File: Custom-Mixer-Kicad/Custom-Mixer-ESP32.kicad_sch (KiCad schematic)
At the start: 20 parts, among them J1 OLED1, J2 OLED2, J3 OLED3, J4 OLED4, J5 OLED5, SW1 RotaryEncoder_Switch, SW2 RotaryEncoder_Switch, U1 ESP32-DevKitC, U2 2717

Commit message: Add +3V3 power symbols and update PCB routing
Added multiple +3V3 power symbols to the schematic for improved clarity and power distribution. Updated PCB routing for nets 1 and 7, including new segments, vias, and changes to net connections for better signal integrity and layout. Adjusted positions of Hackclublogo footprints.
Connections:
- net +3V3: now also RV1.3, RV2.3, RV3.3, RV4.3, RV5.3

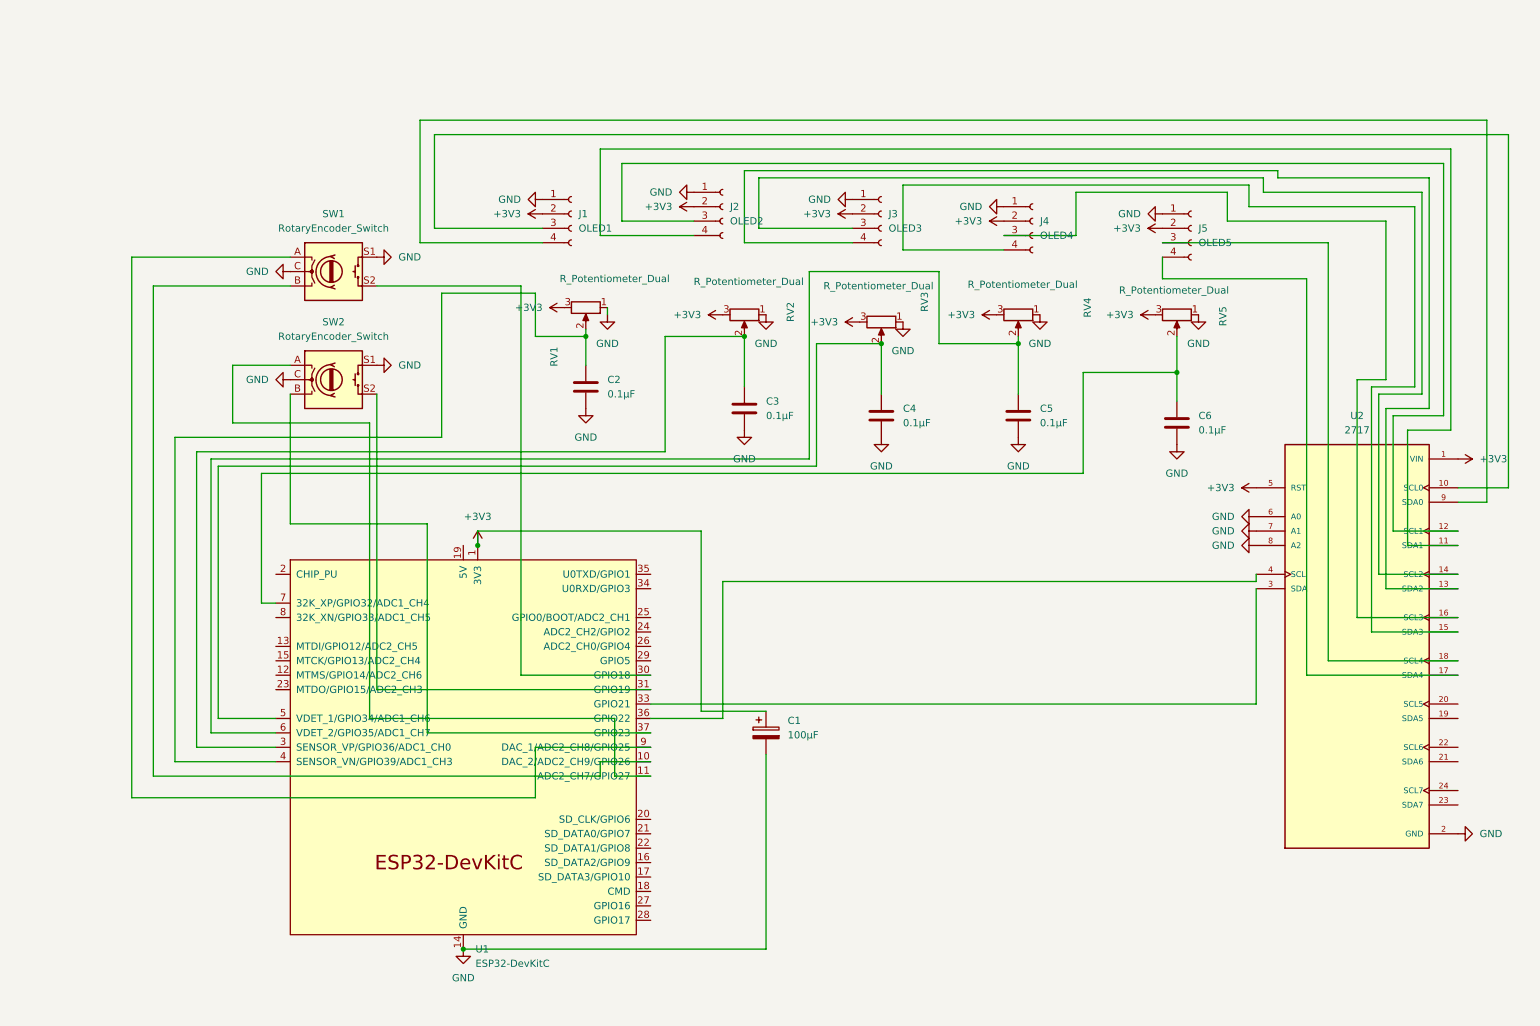
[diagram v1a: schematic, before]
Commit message: Add MCP23017 PCB project & update KiCad libs
Add Adafruit MCP23017 GPIO Expander KiCad project (board, schematic, MCP23017 symbol/footprint, README, license, assets and pretty library parts). Add OLED 128x64 symbol/module files. Modify Custom-Mixer-ESP32 schematic and PCB, and update fp-lib-table and sym-lib-table to include the new parts and libraries.
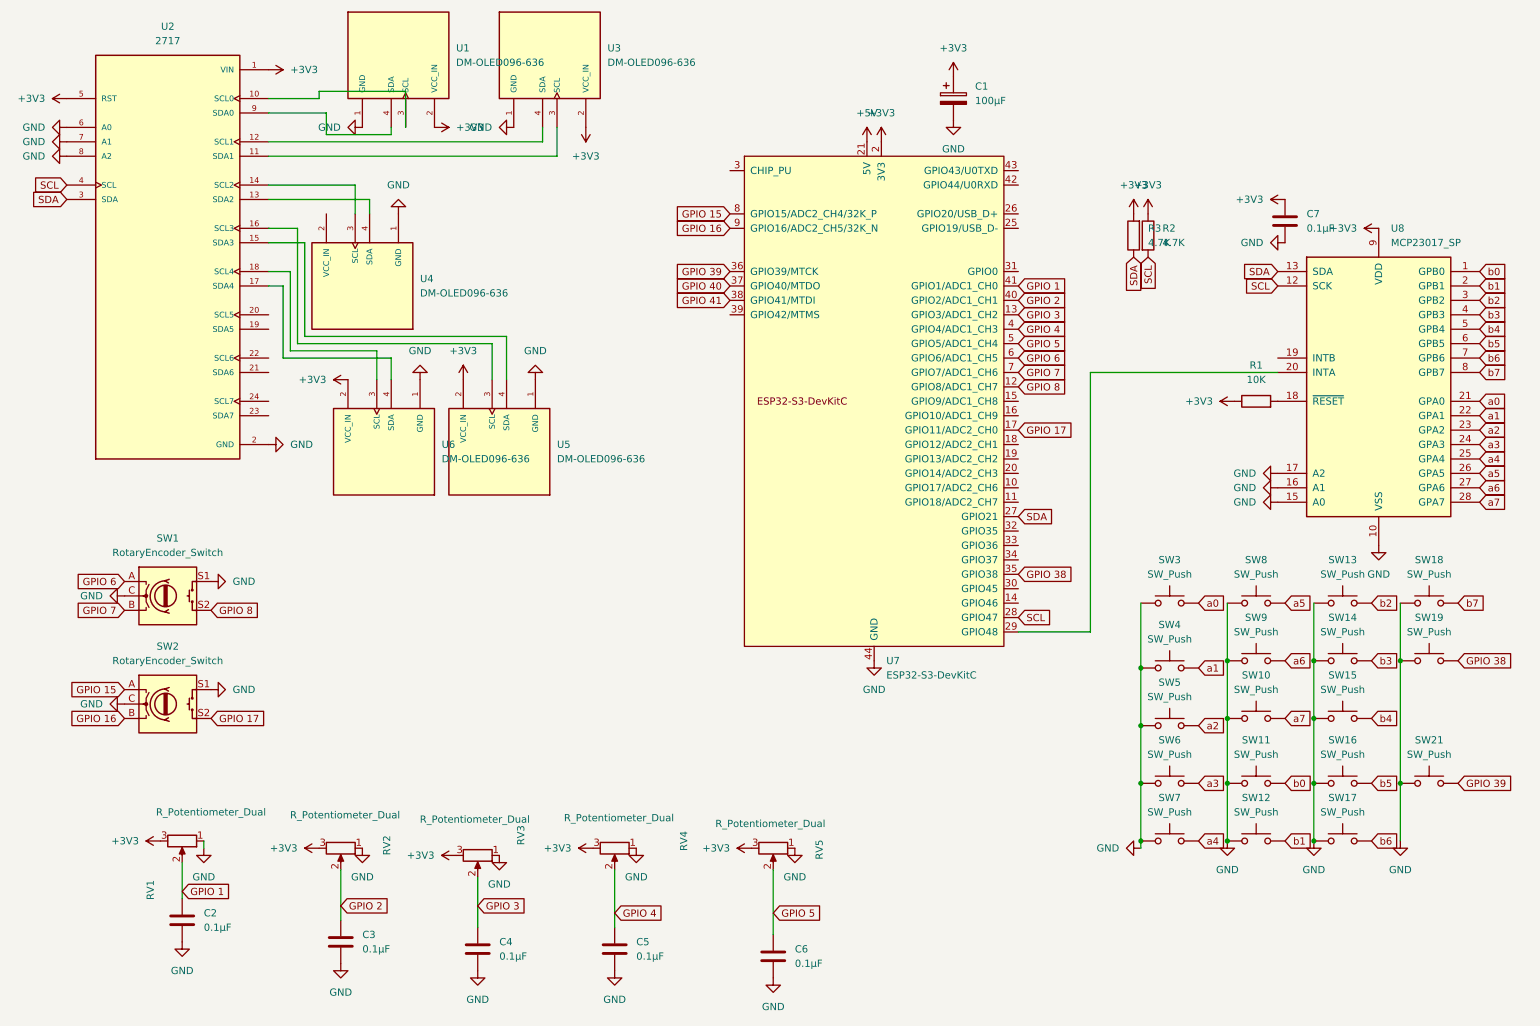
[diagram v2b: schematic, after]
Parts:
- removed J1: OLED1, KiCad-SSD1306-0.91-OLED-4pin-128x32:SSD1306-0.91-OLED-4pin-128x32, symbol Connector:Conn_01x04_Socket
- removed J2: OLED2, KiCad-SSD1306-0.91-OLED-4pin-128x32:SSD1306-0.91-OLED-4pin-128x32, symbol Connector:Conn_01x04_Socket
- removed J3: OLED3, KiCad-SSD1306-0.91-OLED-4pin-128x32:SSD1306-0.91-OLED-4pin-128x32, symbol Connector:Conn_01x04_Socket
- removed J4: OLED4, KiCad-SSD1306-0.91-OLED-4pin-128x32:SSD1306-0.91-OLED-4pin-128x32, symbol Connector:Conn_01x04_Socket
- removed J5: OLED5, KiCad-SSD1306-0.91-OLED-4pin-128x32:SSD1306-0.91-OLED-4pin-128x32, symbol Connector:Conn_01x04_Socket
- removed U1: ESP32-DevKitC, PCM_Espressif:ESP32-DevKitC, symbol PCM_Espressif:ESP32-DevKitC
- added C7: 0.1µF, Capacitor_THT:C_Disc_D5.0mm_W2.5mm_P2.50mm, symbol Device:C
- added R1: 10K, Resistor_THT:R_Axial_DIN0207_L6.3mm_D2.5mm_P7.62mm_Horizontal, symbol Device:R
- added R2, R3: 4.7K, Resistor_THT:R_Axial_DIN0207_L6.3mm_D2.5mm_P7.62mm_Horizontal, symbol Device:R
- added SW10, SW11, SW12, SW13, SW14, SW15, SW16, SW17, SW18, SW19, SW21, SW3, SW4, SW5, SW6, SW7, SW8, SW9: SW_Push, Button_Switch_Keyboard:SW_Cherry_MX_1.00u_PCB, symbol Switch:SW_Push
- added U1, U3, U4, U5, U6: DM-OLED096-636, Oled Screen 128x64:MODULE_DM-OLED096-636, symbol DM-OLED096-636:DM-OLED096-636
- added U7: ESP32-S3-DevKitC, PCM_Espressif:ESP32-S3-DevKitC, symbol PCM_Espressif:ESP32-S3-DevKitC
- added U8: MCP23017_SP, Package_DIP:DIP-28_W7.62mm, symbol Interface_Expansion:MCP23017_SP
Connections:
- net +3V3: now also C7.1, R1.1, R2.1, R3.2, U1.2 (VCC_IN), U3.2 (VCC_IN), U5.2 (VCC_IN), U6.2 (VCC_IN), U7.1 (3V3), U7.2 (3V3), U8.9 (VDD)
- net GND: now also C7.2, SW10.1, SW11.1, SW12.1, SW13.1, SW14.1, SW15.1, SW16.1, SW17.1, SW18.1, SW19.1, SW21.1, SW3.1, SW4.1, SW5.1, SW6.1, SW7.1, SW8.1, SW9.1, U1.1 (GND), U3.1 (GND), U4.1 (GND), U5.1 (GND), U6.1 (GND), U7.22 (GND), U7.23 (GND), U7.24 (GND), U7.44 (GND), U8.10 (VSS), U8.15 (A0), U8.16 (A1), U8.17 (A2)
- net GPIO 3: now reaches C4.1, RV3.2
- net GPIO 3: now also U7.13 (GPIO3/ADC1_CH2)
- net GPIO 4: now reaches C5.1, RV4.2
- net GPIO 4: now also U7.4 (GPIO4/ADC1_CH3)
- net at U2.14 (SCL2): now also U4.3 (SCL)
- net at U2.13 (SDA2): now also U4.4 (SDA)
- net GPIO 2: now reaches C3.1, RV2.2
- net GPIO 2: now also U7.40 (GPIO2/ADC1_CH1)
- net at U2.10 (SCL0): now also U1.3 (SCL)
- net at U2.9 (SDA0): now also U1.4 (SDA)
- net GPIO 5: now reaches C6.1, RV5.2
- net GPIO 5: now also U7.5 (GPIO5/ADC1_CH4)
- net at U2.11 (SDA1): now also U3.3 (SCL)
- net at U2.12 (SCL1): now also U3.4 (SDA)
- net at U2.15 (SDA3): now also U5.4 (SDA)
- net at U2.16 (SCL3): now also U5.3 (SCL)
- net at U2.17 (SDA4): now also U6.4 (SDA)
- net at U2.18 (SCL4): now also U6.3 (SCL)
- net SDA: now reaches U2.3 (SDA)
- net SDA: now also R3.1, U7.27 (GPIO21), U8.13 (SDA)
- net SCL: now reaches U2.4 (SCL)
- net SCL: now also R2.2, U7.28 (GPIO47), U8.12 (SCK)
- net GPIO 7: now reaches SW1.B
- net GPIO 7: now also U7.7 (GPIO7/ADC1_CH6)
- net GPIO 15: now reaches SW2.A
- net GPIO 15: now also U7.8 (GPIO15/ADC2_CH4/32K_P)
- net GPIO 8: now reaches SW1.S2
- net GPIO 8: now also U7.12 (GPIO8/ADC1_CH7)
- net GPIO 17: now reaches SW2.S2
- net GPIO 17: now also U7.17 (GPIO11/ADC2_CH0)
- net GPIO 16: now reaches SW2.B
- net GPIO 16: now also U7.9 (GPIO16/ADC2_CH5/32K_N)
- net GPIO 1: now reaches C2.1, RV1.2
- net GPIO 1: now also U7.41 (GPIO1/ADC1_CH0)
- net GPIO 6: now reaches SW1.A
- net GPIO 6: now also U7.6 (GPIO6/ADC1_CH5)
- new net: U7.29 (GPIO48), U8.20 (INTA)
- new net: R1.2, U8.18 (~{RESET})
- new net +5V: U7.21 (5V)
- new net GPIO 38: SW19.2, U7.35 (GPIO38)
- new net GPIO 39: SW21.2, U7.36 (GPIO39/MTCK)
- new net GPIO 40: U7.37 (GPIO40/MTDO)
- new net GPIO 41: U7.38 (GPIO41/MTDI)
- new net a0: SW3.2, U8.21 (GPA0)
- new net a1: SW4.2, U8.22 (GPA1)
- new net a2: SW5.2, U8.23 (GPA2)
- new net a3: SW6.2, U8.24 (GPA3)
- new net a4: SW7.2, U8.25 (GPA4)
- new net a5: SW8.2, U8.26 (GPA5)
- new net a6: SW9.2, U8.27 (GPA6)
- new net a7: SW10.2, U8.28 (GPA7)
- new net b0: SW11.2, U8.1 (GPB0)
- new net b1: SW12.2, U8.2 (GPB1)
- new net b2: SW13.2, U8.3 (GPB2)
- new net b3: SW14.2, U8.4 (GPB3)
- new net b4: SW15.2, U8.5 (GPB4)
- new net b5: SW16.2, U8.6 (GPB5)
- new net b6: SW17.2, U8.7 (GPB6)
- new net b7: SW18.2, U8.8 (GPB7)
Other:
- moved on the sheet: C1, C2, C3, C4, C5, C6, RV1, RV2, RV3, RV4, RV5, SW1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

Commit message: Rewire and create custom footprint
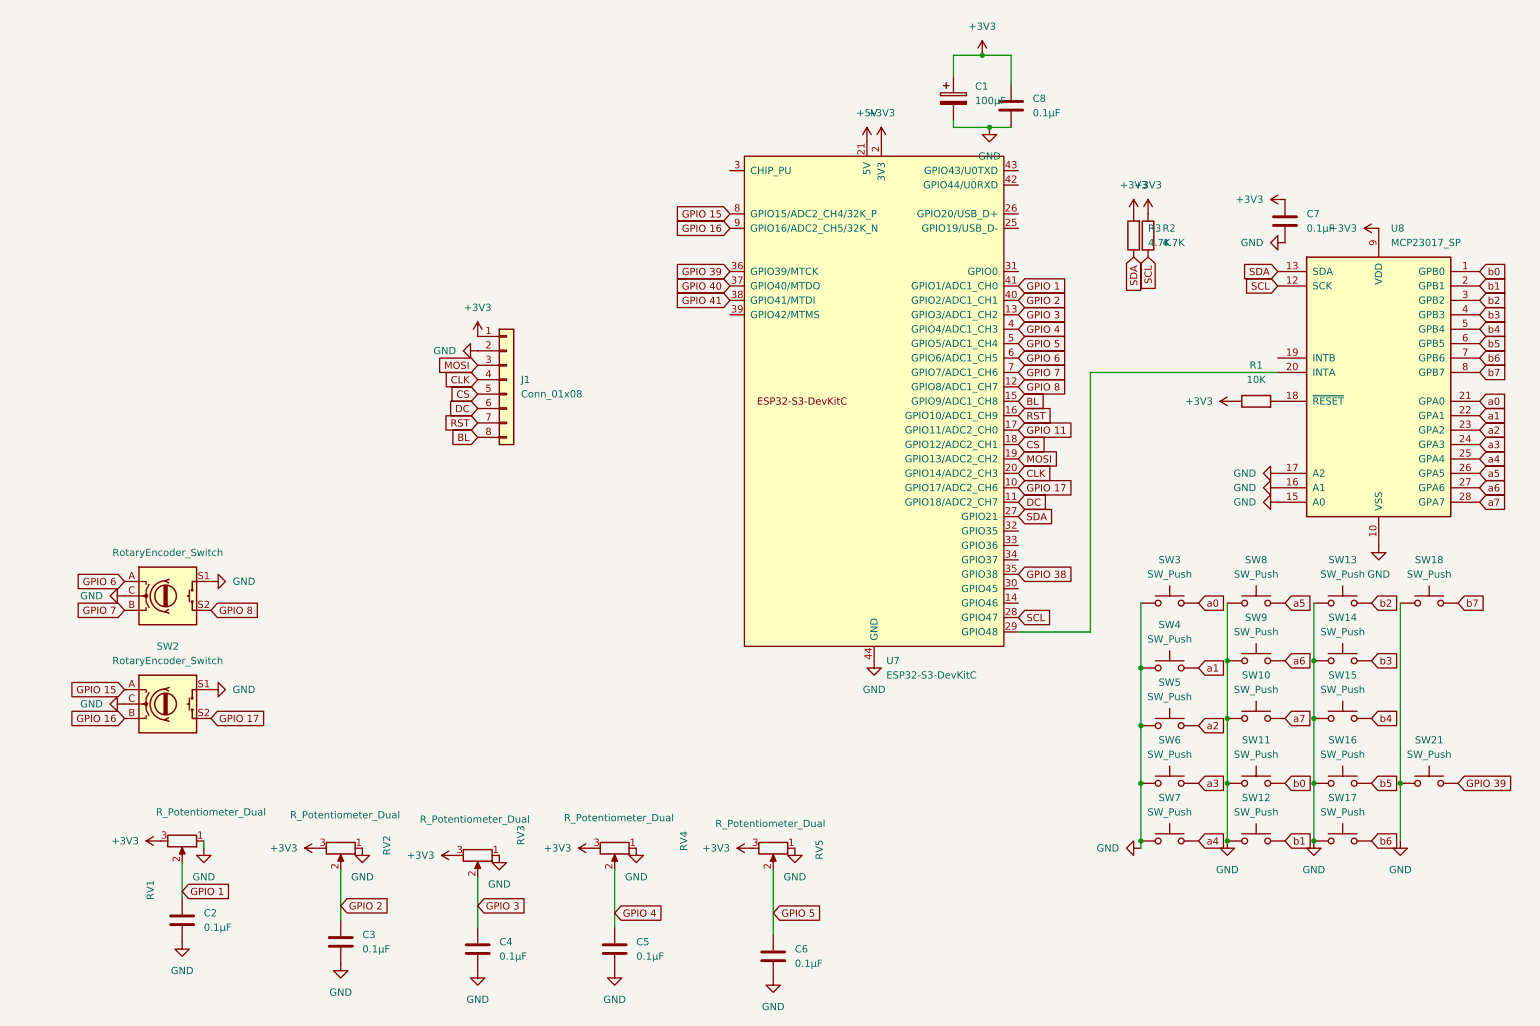
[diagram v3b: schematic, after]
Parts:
- removed SW19: SW_Push, Button_Switch_Keyboard:SW_Cherry_MX_1.00u_PCB, symbol Switch:SW_Push
- removed U1, U3, U4, U5, U6: DM-OLED096-636, Oled Screen 128x64:MODULE_DM-OLED096-636, symbol DM-OLED096-636:DM-OLED096-636
- removed U2: 2717, TCA9548A Breakout:MODULE_2717, symbol 2717:2717
- added C8: 0.1µF, Capacitor_THT:C_Disc_D5.0mm_W2.5mm_P2.50mm, symbol Device:C
- added J1: Conn_01x08, Connector_PinHeader_2.54mm:PinHeader_1x08_P2.54mm_Vertical, symbol Connector_Generic:Conn_01x08
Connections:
- net +3V3: now also C8.1, J1.1 (Pin_1)
- net GND: now also C8.2, J1.2 (Pin_2)
- net GPIO 17: now also U7.10 (GPIO17/ADC2_CH6); no longer U7.17 (GPIO11/ADC2_CH0)
- net DC: now reaches U7.11 (GPIO18/ADC2_CH7)
- net DC: now also J1.6 (Pin_6)
- net BL: now reaches U7.15 (GPIO9/ADC1_CH8)
- net BL: now also J1.8 (Pin_8)
- net RST: now reaches U7.16 (GPIO10/ADC1_CH9)
- net RST: now also J1.7 (Pin_7)
- net CS: now reaches U7.18 (GPIO12/ADC2_CH1)
- net CS: now also J1.5 (Pin_5)
- net MOSI: now reaches U7.19 (GPIO13/ADC2_CH2)
- net MOSI: now also J1.3 (Pin_3)
- net CLK: now reaches U7.20 (GPIO14/ADC2_CH3)
- net CLK: now also J1.4 (Pin_4)
- new net GPIO 11: U7.17 (GPIO11/ADC2_CH0)

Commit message: Complete Wire Revamp
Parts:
- added SW19: SW_Push, Button_Switch_Keyboard:SW_Cherry_MX_1.00u_PCB, symbol Switch:SW_Push
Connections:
- net GND: now also SW19.1
- net GPIO 40: now also SW19.2
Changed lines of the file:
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@@
 	)
 	(junction
+		(at 257.81 127)
+		(diameter 0)
+		(color 0 0 0 0)
+	)
+	(junction
 		(at 242.57 158.75)
 		(diameter 0)
@@
 	(wire
 		(pts
-			(xy 257.81 116.84) (xy 257.81 148.59)
+			(xy 257.81 116.84) (xy 257.81 127)
 		)
 		(stroke
@@
 	(wire
 		(pts
+			(xy 257.81 127) (xy 257.81 148.59)
+		)
+		(stroke
+			(width 0)
+			(type default)
+		)
+	)
+	(wire
+		(pts
 			(xy 119.38 163.83) (xy 119.38 173.99)
 		)
@@
 		)
 	)
+	(global_label "GPIO 40"
+		(shape input)
+		(at 267.97 127 0)
+		(fields_autoplaced yes)
+		(effects
+			(font
+				(size 1.27 1.27)
+			)
+			(justify left)
+		)
+		(property "Intersheetrefs" "${INTERSHEET_REFS}"
+			(at 278.8171 127 0)
+			(effects
+				(font
+					(size 1.27 1.27)
+				)
+				(justify left)
+				(hide yes)
+			)
+		)
+	)
 	(symbol
 		(lib_id "power:GND")
@@
 					(unit 1)
 				)
+			)
+		)
+	)
+	(symbol
+		(lib_id "Switch:SW_Push")
+		(at 262.89 127 0)
+		(unit 1)
+		(exclude_from_sim no)
+		(in_bom yes)
+		(on_board yes)
+		(dnp no)
+		(fields_autoplaced yes)
+		(property "Reference" "SW19"
+			(at 262.89 119.38 0)
+			(effects
+				(font
+					(size 1.27 1.27)
+				)
+			)
+		)
+		(property "Value" "SW_Push"
+			(at 262.89 121.92 0)
+			(effects
+				(font
+					(size 1.27 1.27)
+				)
+			)
+		)
+		(property "Footprint" "Button_Switch_Keyboard:SW_Cherry_MX_1.00u_PCB"
+			(at 262.89 121.92 0)
+			(effects
+				(font
+					(size 1.27 1.27)
+				)
+				(hide yes)
+			)
+		)
+		(property "Datasheet" "~"
+			(at 262.89 121.92 0)
+			(effects
+				(font
+					(size 1.27 1.27)
+				)
+				(hide yes)
+			)
+		)
+		(property "Description" "Push button switch, generic, two pins"
+			(at 262.89 127 0)
+			(effects
+				(font
+					(size 1.27 1.27)
+				)
+				(hide yes)
+			)
+		)
+		(pin "2"
+		)
+		(pin "1"
+		)
+		(instances
+			(project "Custom-Mixer-ESP32"
+				(path "/73629794-8790-492e-bf38-e26558ab2153"
+					(reference "SW19")
+					(unit 1)
+				)

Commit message: PCB rework completed
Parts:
- J1: footprint Connector_PinHeader_2.54mm:PinHeader_1x08_P2.54mm_Vertical -> Connector_PinSocket_2.54mm:PinSocket_1x09_P2.54mm_Vertical; symbol Connector_Generic:Conn_01x08 -> Connector_Generic:Conn_01x09
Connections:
- net CLK: now also J1.7 (Pin_7); no longer J1.4 (Pin_4)
- net CS: now also J1.3 (Pin_3); no longer J1.5 (Pin_5)
- net DC: now also J1.5 (Pin_5); no longer J1.6 (Pin_6)
- net MOSI: now also J1.6 (Pin_6); no longer J1.3 (Pin_3)
- net RST: now also J1.4 (Pin_4); no longer J1.7 (Pin_7)
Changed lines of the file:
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@@
 	(global_label "RST"
 		(shape input)
-		(at 95.25 85.09 180)
+		(at 95.25 77.47 180)
 		(fields_autoplaced yes)
 		(effects
@@
 		)
 		(property "Intersheetrefs" "${INTERSHEET_REFS}"
-			(at 88.8177 85.09 0)
+			(at 88.8177 77.47 0)
 			(effects
 				(font
@@
 	(global_label "CS"
 		(shape input)
-		(at 95.25 80.01 180)
+		(at 95.25 74.93 180)
 		(fields_autoplaced yes)
 		(effects
@@
 		)
 		(property "Intersheetrefs" "${INTERSHEET_REFS}"
-			(at 89.7853 80.01 0)
+			(at 89.7853 74.93 0)
 			(effects
 				(font
@@
 	(global_label "CLK"
 		(shape input)
-		(at 95.25 77.47 180)
+		(at 95.25 85.09 180)
 		(fields_autoplaced yes)
 		(effects
@@
 		)
 		(property "Intersheetrefs" "${INTERSHEET_REFS}"
-			(at 88.6967 77.47 0)
+			(at 88.6967 85.09 0)
 			(effects
 				(font
@@
 	(global_label "DC"
 		(shape input)
-		(at 95.25 82.55 180)
+		(at 95.25 80.01 180)
 		(fields_autoplaced yes)
 		(effects
@@
 		)
 		(property "Intersheetrefs" "${INTERSHEET_REFS}"
-			(at 89.7248 82.55 0)
+			(at 89.7248 80.01 0)
 			(effects
 				(font
@@
 	(global_label "MOSI"
 		(shape input)
-		(at 95.25 74.93 180)
+		(at 95.25 82.55 180)
 		(fields_autoplaced yes)
 		(effects
@@
 		)
 		(property "Intersheetrefs" "${INTERSHEET_REFS}"
-			(at 87.6686 74.93 0)
+			(at 87.6686 82.55 0)
 			(effects
 				(font
@@
 	)
 	(symbol
-		(lib_id "Connector_Generic:Conn_01x08")
-		(at 100.33 77.47 0)
+		(lib_id "Connector_Generic:Conn_01x09")
+		(at 100.33 80.01 0)
 		(unit 1)
 		(exclude_from_sim no)
@@
 		(fields_autoplaced yes)
 		(property "Reference" "J1"
-			(at 102.87 77.4699 0)
+			(at 102.87 78.7399 0)
 			(effects
 				(font
@@
 		)
 		(property "Value" "Conn_01x08"
-			(at 102.87 80.0099 0)
+			(at 102.87 81.2799 0)
 			(effects
 				(font
@@
 			)
 		)
-		(property "Footprint" "Connector_PinHeader_2.54mm:PinHeader_1x08_P2.54mm_Vertical"
-			(at 100.33 77.47 0)
+		(property "Footprint" "Connector_PinSocket_2.54mm:PinSocket_1x09_P2.54mm_Vertical"
+			(at 100.33 80.01 0)
 			(effects
 				(font
@@
 		)
 		(property "Datasheet" "~"
-			(at 100.33 77.47 0)
+			(at 100.33 80.01 0)
 			(effects
 				(font
@@
 			)
 		)
-		(property "Description" "Generic connector, single row, 01x08, script generated (kicad-library-utils/schlib/autogen/connector/)"
-			(at 100.33 77.47 0)
+		(property "Description" "Generic connector, single row, 01x09, script generated (kicad-library-utils/schlib/autogen/connector/)"
+			(at 100.33 80.01 0)
 			(effects
 				(font
@@
 		(pin "1"
 		)
+		(pin "9"
+		)
 		(instances
